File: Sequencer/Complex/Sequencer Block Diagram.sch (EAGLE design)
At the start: 1 part, among them IC1 74386N

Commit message: Work on state diagram
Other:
- note added: "(LCK1)' = '0'"
- note added: "(LCK1)' = '1'"
- note added: "(LCK2)' = '0'"
- note added: "(LCK2)' = '1'"
- note added: "(Output Enable)' = '0'"
- note added: "(Output Enable)' = 'X'"
- note added: "(Write Enable)' = 'X'"
- note added: "All if INT = (10)'"
- note added: "EN0 = '0'"
- note added: "EN0 = '1'"
- note added: "EN0 = 0"
- note added: "EN1 = '0'"
- note added: "EN1 = 'X'"
- note added: "INT = "10""
- note added: "INT = (10)'"
- note added: "INT ="00""
- note added: "LOAD = '0'"
- note added: "LOAD = '1'"
- note added: "READ/PNR/RESET = '0'"
- note added: "READ/PNR/RESET = 'X'"
- note added: "S5"
- note added: "S6"
- note added: "Toggle = '0'"
- note added: "Toggle = '1'"
- note added: "Write Buffer to Memory"
- note added: "Write Zeros to RAM State Diagram"
- note removed: "(Output Enable)' = '1'"
- note removed: "LCK2 = '0'"
- note removed: "LCK2 = '1'"
- note removed: "Write Zeros to RAM State Machine"

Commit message: update State diagram
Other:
- note added: "(LCK0)' = '0'"
- note added: "(LCK0)' = '1'"
- note added: "ALL if INT = (01)'"
- note added: "Don't change S1-S5"
- note added: "EN0 = "X""
- note added: "EN1 = "0""
- note added: "EN1 = "1""
- note added: "INT = "01""
- note added: "INT = (01)'"
- note added: "LOAD/PNR/RESET = '0'"
- note added: "LOAD/PNR/RESET = 'X'"
- note added: "Loading From RAM into Buffer"
- note added: "READ = '0'"
- note added: "Toggle = 'X'"
- note added: "X"
- note removed: "(LCK1)' = '1'"
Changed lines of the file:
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@@
 <part name="FRAME3" library="frames" library_urn="urn:adsk.eagle:library:229" deviceset="FRAME_A_L" device=""/>
 <part name="FRAME4" library="frames" library_urn="urn:adsk.eagle:library:229" deviceset="FRAME_A_L" device=""/>
+<part name="FRAME5" library="frames" library_urn="urn:adsk.eagle:library:229" deviceset="FRAME_A_L" device=""/>
 </parts>
 <sheets>
@@
 <circle x="142.24" y="129.54" radius="7.62" width="0.1524" layer="94"/>
 <text x="63.5" y="162.56" size="1.778" layer="94">LOAD = '0'</text>
-<text x="63.5" y="170.18" size="1.778" layer="94">(LCK1)' = '0'</text>
+<text x="63.5" y="170.18" size="1.778" layer="94">(LCK0)' = '0'</text>
 <text x="152.4" y="160.02" size="1.778" layer="94">LOAD = '1'</text>
-<text x="152.4" y="157.48" size="1.778" layer="94">Toggle = '1'</text>
-<text x="152.4" y="162.56" size="1.778" layer="94">(LCK1)' = '1'</text>
-<text x="167.64" y="162.56" size="1.778" layer="94">EN0 = '1'</text>
-<text x="167.64" y="160.02" size="1.778" layer="94">EN1 = '0'</text>
+<text x="152.4" y="154.94" size="1.778" layer="94">Toggle = '1'</text>
+<text x="152.4" y="162.56" size="1.778" layer="94">(LCK0)' = '1'</text>
+<text x="152.4" y="147.32" size="1.778" layer="94">EN0 = '1'</text>
+<text x="152.4" y="149.86" size="1.778" layer="94">EN1 = '0'</text>
 <text x="152.4" y="152.4" size="1.778" layer="94">(Write Enable)' = '0'</text>
-<text x="152.4" y="149.86" size="1.778" layer="94">(Output Enable)' = '0'</text>
-<text x="152.4" y="167.64" size="1.778" layer="94">READ/PNR/RESET = '0'</text>
+<text x="152.4" y="167.64" size="1.778" layer="94">(Output Enable)' = '0'</text>
+<text x="152.4" y="165.1" size="1.778" layer="94">READ/PNR/RESET = '0'</text>
 <text x="140.716" y="128.524" size="1.778" layer="94">S2</text>
 <wire x1="66.04" y1="152.4" x2="76.2" y2="152.4" width="0.1524" layer="94"/>
@@
 <text x="152.4" y="132.08" size="1.778" layer="94">(Write Enable)' = '0'</text>
 <text x="127" y="137.16" size="1.778" layer="94">INT = "10"</text>
-<text x="152.4" y="129.54" size="1.778" layer="94">Toggle = '1'</text>
+<text x="152.4" y="129.54" size="1.778" layer="94">Toggle = '0'</text>
 <circle x="142.24" y="106.68" radius="7.62" width="0.1524" layer="94"/>
 <wire x1="142.24" y1="121.92" x2="142.24" y2="114.3" width="0.1524" layer="94"/>
@@
 <wire x1="96.52" y1="121.92" x2="93.98" y2="119.38" width="0.1524" layer="94"/>
 <wire x1="96.52" y1="121.92" x2="99.06" y2="119.38" width="0.1524" layer="94"/>
-<wire x1="102.616" y1="134.62" x2="136.652" y2="147.32" width="0.1524" layer="94" curve="-38.893711"/>
-<wire x1="109.728" y1="139.7" x2="108.712" y2="139.7" width="0.1524" layer="94"/>
-<wire x1="109.728" y1="139.7" x2="109.22" y2="138.684" width="0.1524" layer="94"/>
-<text x="106.68" y="134.62" size="1.778" layer="94">INT = "10"</text>
-<text x="83.82" y="139.7" size="1.778" layer="94">INT = (10)'</text>
 <text x="127" y="119.38" size="1.778" layer="94">INT = "10"</text>
 <text x="102.87" y="112.014" size="1.778" layer="94">INT = "10"</text>
@@
 <text x="55.88" y="175.26" size="1.778" layer="94">(Write Enable)' = 'X'</text>
 <text x="55.88" y="172.72" size="1.778" layer="94">(Output Enable)' = 'X'</text>
+<text x="152.4" y="106.68" size="1.778" layer="94">Toggle = '0'</text>
+<text x="114.3" y="93.98" size="1.778" layer="94">Toggle = '0'</text>
+<text x="73.66" y="106.68" size="1.778" layer="94">Toggle = '0'</text>
+<text x="73.66" y="134.62" size="1.778" layer="94">Toggle = '0'</text>
+<text x="66.04" y="104.14" size="1.778" layer="94">(Write Enable)' = '0'</text>
+<text x="114.3" y="91.44" size="1.778" layer="94">(Write Enable)' = '1'</text>
+<wire x1="181.864" y1="170.18" x2="182.88" y2="170.18" width="0.1524" layer="94"/>
+<wire x1="182.88" y1="160.02" x2="182.88" y2="170.18" width="0.1524" layer="94"/>
+<wire x1="182.88" y1="160.02" x2="182.118" y2="160.02" width="0.1524" layer="94"/>
+<text x="185.42" y="162.56" size="1.778" layer="94">Don't change
+S1-S5</text>
+<text x="66.04" y="132.08" size="1.778" layer="94">(Write Enable)' = '0'</text>
+<text x="73.66" y="129.54" size="1.778" layer="94">(LCK1)' = '0'</text>
+<text x="73.66" y="127" size="1.778" layer="94">LOAD = '0'</text>
+<text x="60.96" y="124.46" size="1.778" layer="94">READ/PNR/RESET = '0'</text>
+<text x="66.04" y="121.92" size="1.778" layer="94">(Output Enable)' = '0'</text>
+<text x="93.98" y="139.7" size="1.778" layer="94">X</text>
 </plain>
 <instances>
@@
 <attribute name="LAST_DATE_TIME" x="185.42" y="1.27" size="2.54" layer="94"/>
 <attribute name="SHEET" x="259.08" y="1.27" size="2.54" layer="94"/>
+<attribute name="DRAWING_NAME" x="190.5" y="19.05" size="2.54" layer="94"/>
+</instance>
+</instances>
+<busses>
+</busses>
+<nets>
+</nets>
+</sheet>
+<sheet>
+<plain>
+<text x="101.6" y="177.8" size="1.778" layer="94">Loading From RAM
+into Buffer</text>
+<circle x="81.28" y="160.02" radius="7.62" width="0.1524" layer="94"/>
+<text x="79.756" y="159.258" size="1.778" layer="94">S0</text>
+<circle x="127" y="160.02" radius="7.62" width="0.1524" layer="94"/>
+<text x="125.222" y="159.258" size="1.778" layer="94">S1</text>
+<circle x="127" y="134.62" radius="7.62" width="0.1524" layer="94"/>
+<circle x="104.14" y="134.62" radius="7.62" width="0.1524" layer="94"/>
+<circle x="81.28" y="134.62" radius="7.62" width="0.1524" layer="94"/>
+<wire x1="88.9" y1="134.62" x2="91.44" y2="137.16" width="0.1524" layer="94"/>
+<wire x1="88.9" y1="134.62" x2="91.44" y2="132.08" width="0.1524" layer="94"/>
+<wire x1="88.9" y1="134.62" x2="96.52" y2="134.62" width="0.1524" layer="94"/>
+<wire x1="111.76" y1="134.62" x2="119.38" y2="134.62" width="0.1524" layer="94"/>
+<wire x1="111.76" y1="134.62" x2="114.3" y2="137.16" width="0.1524" layer="94"/>
+<wire x1="111.76" y1="134.62" x2="114.3" y2="132.08" width="0.1524" layer="94"/>
+<wire x1="127" y1="152.4" x2="127" y2="142.24" width="0.1524" layer="94"/>
+<wire x1="127" y1="142.24" x2="129.54" y2="144.78" width="0.1524" layer="94"/>
+<wire x1="127" y1="142.24" x2="124.46" y2="144.78" width="0.1524" layer="94"/>
+<wire x1="81.28" y1="152.4" x2="81.28" y2="142.24" width="0.1524" layer="94"/>
+<wire x1="81.28" y1="152.4" x2="83.82" y2="149.86" width="0.1524" layer="94"/>
+<wire x1="81.28" y1="152.4" x2="78.74" y2="149.86" width="0.1524" layer="94"/>
+<text x="125.476" y="133.604" size="1.778" layer="94">S2</text>
+<text x="102.616" y="133.604" size="1.778" layer="94">S3</text>
+<text x="79.756" y="133.858" size="1.778" layer="94">S4</text>
+<wire x1="88.9" y1="160.02" x2="119.38" y2="160.02" width="0.1524" layer="94"/>
+<wire x1="119.38" y1="160.02" x2="116.84" y2="162.56" width="0.1524" layer="94"/>
+<wire x1="119.38" y1="160.02" x2="116.84" y2="157.48" width="0.1524" layer="94"/>
+<text x="99.06" y="162.56" size="1.778" layer="94">INT = "01"</text>
+<text x="114.3" y="147.32" size="1.778" layer="94">INT = "01"</text>
+<text x="110.236" y="139.7" size="1.778" layer="94">INT = "01"</text>
+<text x="87.122" y="138.938" size="1.778" layer="94">INT = "01"</text>
+<wire x1="73.66" y1="160.02" x2="63.5" y2="160.02" width="0.1524" layer="94"/>
+<wire x1="63.5" y1="160.02" x2="63.5" y2="175.26" width="0.1524" layer="94"/>
+<wire x1="63.5" y1="175.26" x2="81.28" y2="175.26" width="0.1524" layer="94"/>
+<wire x1="81.28" y1="175.26" x2="81.28" y2="167.64" width="0.1524" layer="94"/>
+<wire x1="81.28" y1="167.64" x2="83.82" y2="170.18" width="0.1524" layer="94"/>
+<wire x1="81.28" y1="167.64" x2="78.74" y2="170.18" width="0.1524" layer="94"/>
+<text x="66.04" y="172.72" size="1.778" layer="94">INT = (01)'</text>
+<text x="78.74" y="147.32" size="1.778" layer="94">X</text>
+<wire x1="63.5" y1="160.02" x2="53.34" y2="160.02" width="0.1524" layer="94"/>
+<text x="45.72" y="157.48" size="1.778" layer="94">ALL if
+INT = (01)'</text>
+<text x="63.5" y="185.42" size="1.778" layer="94">READ = '0'</text>
+<text x="63.5" y="182.88" size="1.778" layer="94">(LCK1)' = '0'</text>
+<text x="63.5" y="180.34" size="1.778" layer="94">Toggle = 'X'</text>
+<text x="63.5" y="177.8" size="1.778" layer="94">LOAD/PNR/RESET = 'X'</text>
+<text x="63.5" y="190.5" size="1.778" layer="94">EN0 = "X"</text>
+<text x="63.5" y="187.96" size="1.778" layer="94">EN1 = "0"</text>
+<text x="137.16" y="172.72" size="1.778" layer="94">EN1 = "1"</text>
+<text x="137.16" y="170.18" size="1.778" layer="94">LOAD/PNR/RESET = '0'</text>
+</plain>
+<instances>
+<instance part="FRAME5" gate="G$1" x="0" y="0" smashed="yes"/>
+<instance part="FRAME5" gate="G$2" x="172.72" y="0" smashed="yes">
+<attribute name="LAST_DATE_TIME" x="185.42" y="1.27" size="2.54" layer="94"/>
+<attribute name="SHEET" x="259.08" y="1.27" size="2.54" layer="94"/>

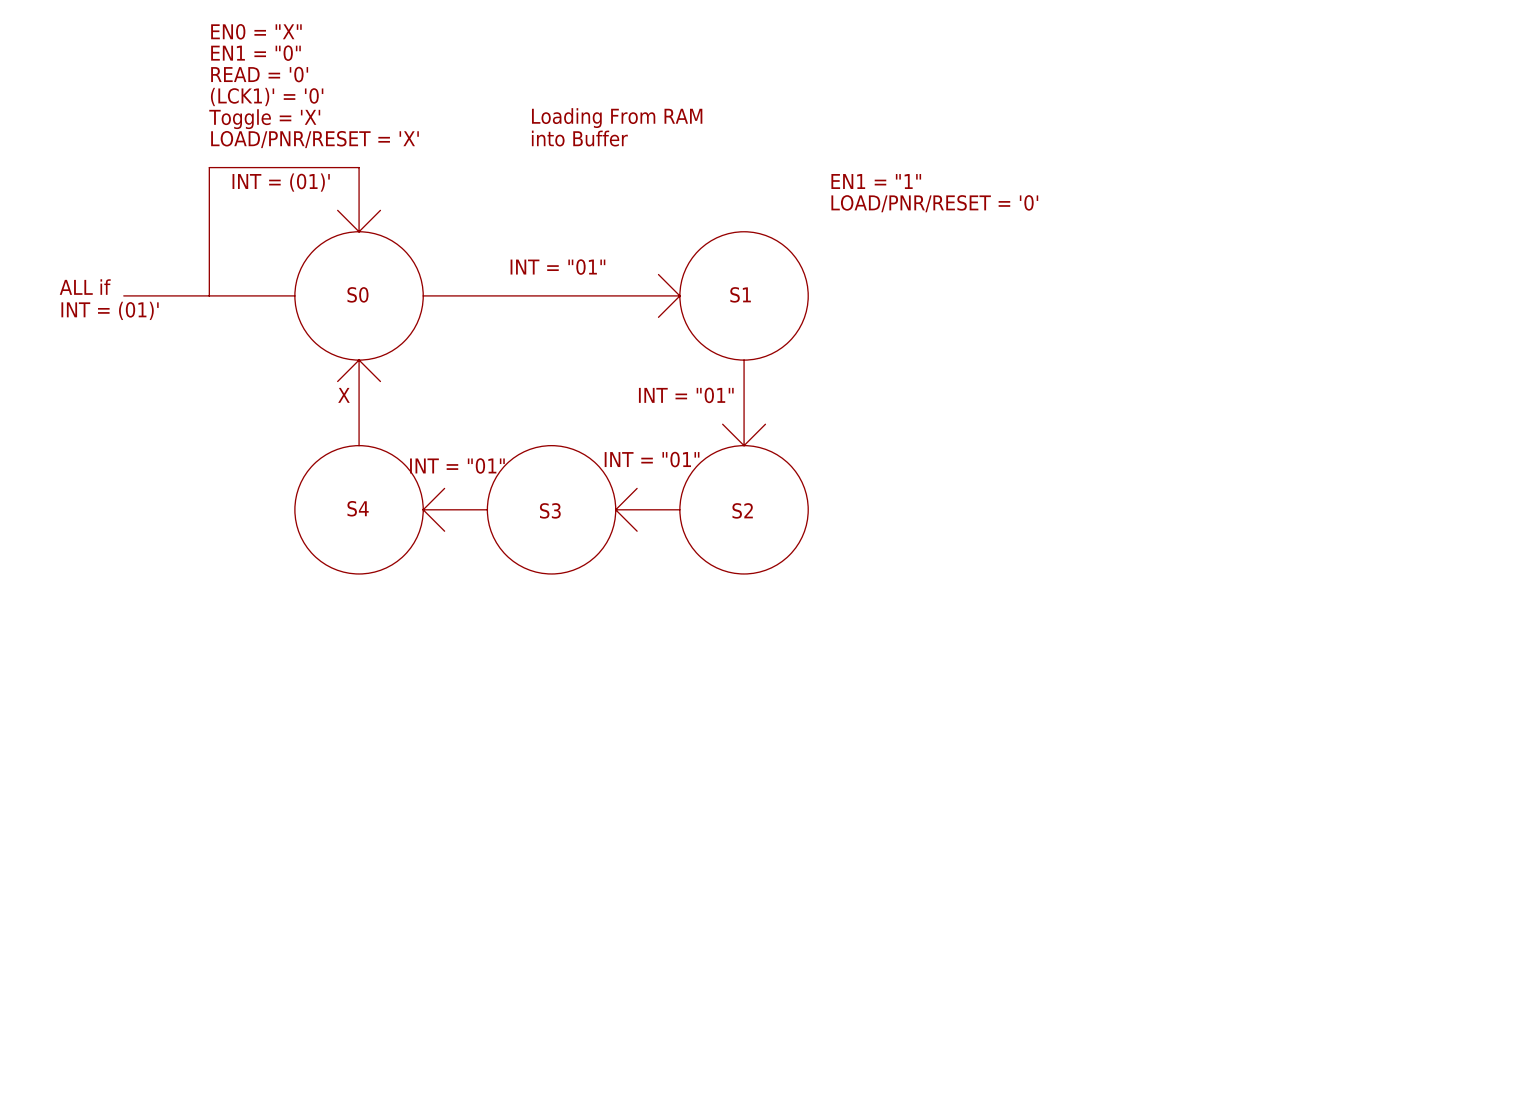
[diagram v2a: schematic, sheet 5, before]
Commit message: updated state diagram
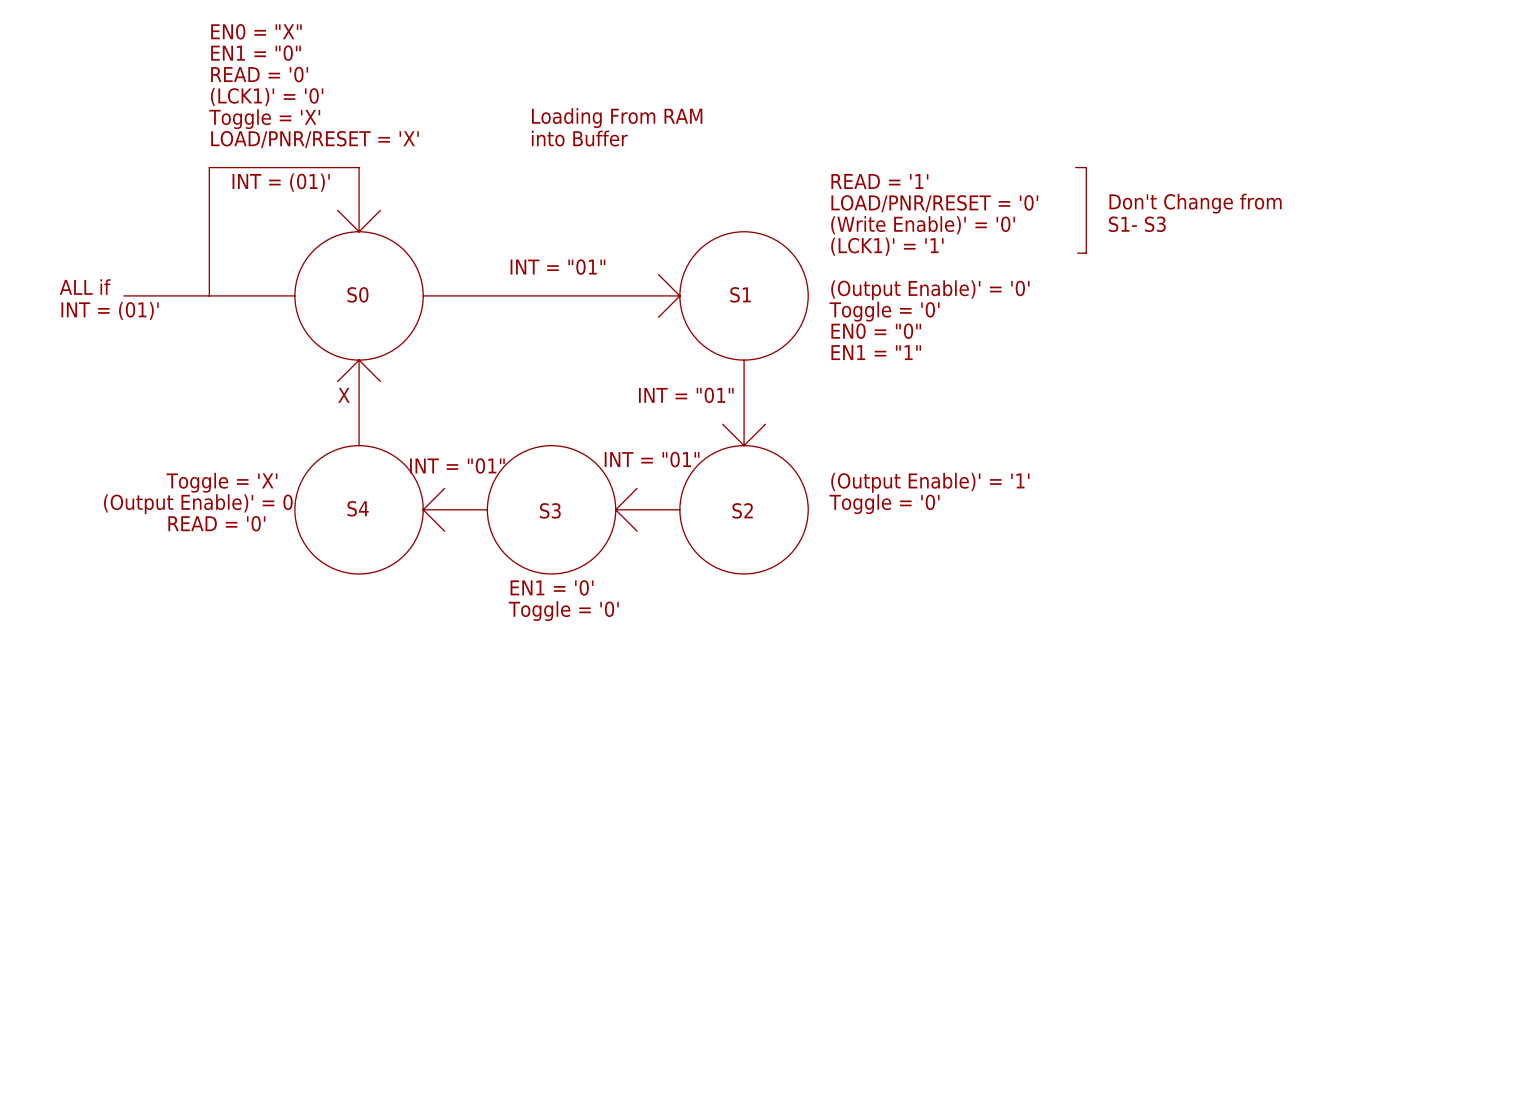
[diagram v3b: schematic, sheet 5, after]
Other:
- note added: "(LCK1)' = '1'"
- note added: "(Output Enable)' = '1'"
- note added: "(Output Enable)' = 0"
- note added: "Don't Change from S1- S3"
- note added: "EN0 = "0""
- note added: "READ = '1'"
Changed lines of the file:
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@@
 <text x="63.5" y="190.5" size="1.778" layer="94">EN0 = "X"</text>
 <text x="63.5" y="187.96" size="1.778" layer="94">EN1 = "0"</text>
-<text x="137.16" y="172.72" size="1.778" layer="94">EN1 = "1"</text>
+<text x="137.16" y="152.4" size="1.778" layer="94">EN1 = "1"</text>
 <text x="137.16" y="170.18" size="1.778" layer="94">LOAD/PNR/RESET = '0'</text>
+<text x="137.16" y="167.64" size="1.778" layer="94">(Write Enable)' = '0'</text>
+<text x="137.16" y="160.02" size="1.778" layer="94">(Output Enable)' = '0'</text>
+<text x="137.16" y="165.1" size="1.778" layer="94">(LCK1)' = '1'</text>
+<text x="137.16" y="154.94" size="1.778" layer="94">EN0 = "0"</text>
+<text x="137.16" y="137.16" size="1.778" layer="94">(Output Enable)' = '1'</text>
+<text x="99.06" y="124.46" size="1.778" layer="94">EN1 = '0'</text>
+<text x="137.16" y="172.72" size="1.778" layer="94">READ = '1'</text>
+<text x="137.16" y="157.48" size="1.778" layer="94">Toggle = '0'</text>
+<text x="137.16" y="134.62" size="1.778" layer="94">Toggle = '0'</text>
+<text x="99.06" y="121.92" size="1.778" layer="94">Toggle = '0'</text>
+<text x="58.42" y="137.16" size="1.778" layer="94">Toggle = 'X'</text>
+<text x="50.8" y="134.62" size="1.778" layer="94">(Output Enable)' = 0</text>
+<text x="58.42" y="132.08" size="1.778" layer="94">READ = '0'</text>
+<wire x1="166.37" y1="175.26" x2="167.64" y2="175.26" width="0.1524" layer="94"/>
+<wire x1="167.64" y1="175.26" x2="167.64" y2="165.1" width="0.1524" layer="94"/>
+<wire x1="167.64" y1="165.1" x2="166.624" y2="165.1" width="0.1524" layer="94"/>
+<text x="170.18" y="167.64" size="1.778" layer="94">Don't Change from
+S1- S3</text>
 </plain>
 <instances>

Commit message: Added to State Diagram
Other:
- note added: "(OE)'"
- note added: "(Output Enable)'"
- note added: "(Reset Timer)' = 1"
- note added: "(Timer) DONE = 0"
- note added: "(WE)'"
- note added: "(Write Enable)'"
- note added: "2-INPUT AND"
- note added: "4-Bit Counter"
- note added: "8 BIT TRI STATE BUFFER"
- note added: "8 to 1 MUX"
- note added: "A7"
- note added: "ADDRESS BUS (7)"
- note added: "ALL if INT = (11)'"
- note added: "BPM CLOCK SIGNAL"
- note added: "BPM COUNTER[6] BPMC(2), BPMC(1), BPMC(0)"
- note added: "Beats Per Second COUNTER (6-bit)"
- note added: "D0"
- note added: "D7"
- note added: "DATABUS (8)"
- note added: "DONE"
- note added: "DONE = '1'"
- note added: "HSB"
- note added: "IDT6116SA"
- note added: "INT = "11""
- note added: "INT = (11)'"
- note added: "LATCH"
- note added: "LATCH = '0'"
- note added: "LATCH = '0' PNR = '0'"
- note added: "LATCH = '1' PNR = '0'"
- note added: "LOAD/READ/RESET = '0'"
- note added: "LSB"
- note added: "Load "Play - Next" Register"
- note added: "PNR"
- note added: "PNR = '0'"
- note added: "PNR = '1'"
- note added: "SHIFT REGISTER W/ OUTPUT REGISTER"
- note added: "SN74AHC594"
- note added: "SN74HC590A"
- note added: "SRAM"
- note added: "This Signal is '0' From S1-S4"
- note added: "To INSTUMENT TRIGGERS"
- note added: "Toggle = "X""
- note added: "Used in MUX"
